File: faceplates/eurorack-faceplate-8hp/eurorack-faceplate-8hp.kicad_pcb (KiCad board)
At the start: 2 copper layers, 40.3 x 133.3 mm, 2 parts

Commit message: Moving mounting holes
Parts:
- added REF**: MountingHole_3.2mm_M3, MountingHole:MountingHole_3.2mm_M3, F.Cu at (35.2, 3.00)
- added REF**: MountingHole_3.2mm_M3, MountingHole:MountingHole_3.2mm_M3, F.Cu at (35.2, 130.3)
- moved REF** 2.42 mm to (5.08, 130.3)
- moved REF** 2.42 mm to (5.08, 3.00)
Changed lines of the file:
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@@
   (net 0 "")
   (footprint "MountingHole:MountingHole_3.2mm_M3" (layer "F.Cu")
-    (at 7.5 130.35)
+    (at 35.22 3)
     (descr "Mounting Hole 3.2mm, no annular, M3")
     (tags "mounting hole 3.2mm no annular m3")
@@
   )
   (footprint "MountingHole:MountingHole_3.2mm_M3" (layer "F.Cu")
-    (at 7.5 3)
+    (at 35.22 130.35)
+    (descr "Mounting Hole 3.2mm, no annular, M3")
+    (tags "mounting hole 3.2mm no annular m3")
+    (attr exclude_from_pos_files exclude_from_bom)
+    (fp_text reference "REF**" (at 0 -4.2) (layer "F.SilkS") hide
+      (effects (font (size 1 1) (thickness 0.15)))
+    )
+    (fp_text value "MountingHole_3.2mm_M3" (at 0 4.2) (layer "F.Fab") hide
+      (effects (font (size 1 1) (thickness 0.15)))
+    )
+    (fp_text user "${REFERENCE}" (at 0.3 0) (layer "F.Fab") hide
+      (effects (font (size 1 1) (thickness 0.15)))
+    )
+    (fp_circle (center 0 0) (end 3.2 0) (layer "Cmts.User") (width 0.15) (fill none))
+    (fp_circle (center 0 0) (end 3.45 0) (layer "F.CrtYd") (width 0.05) (fill none))
+    (pad "" np_thru_hole oval locked (at 0 0) (size 7 3.2) (drill oval 7 3.2) (layers F&B.Cu *.Mask))
+  )
+  (footprint "MountingHole:MountingHole_3.2mm_M3" (layer "F.Cu")
+    (at 5.08 130.35)
+    (descr "Mounting Hole 3.2mm, no annular, M3")
+    (tags "mounting hole 3.2mm no annular m3")
+    (attr exclude_from_pos_files exclude_from_bom)
+    (fp_text reference "REF**" (at 0 -4.2) (layer "F.SilkS") hide
+      (effects (font (size 1 1) (thickness 0.15)))
+    )
+    (fp_text value "MountingHole_3.2mm_M3" (at 0 4.2) (layer "F.Fab") hide
+      (effects (font (size 1 1) (thickness 0.15)))
+    )
+    (fp_text user "${REFERENCE}" (at 0.3 0) (layer "F.Fab") hide
+      (effects (font (size 1 1) (thickness 0.15)))
+    )
+    (fp_circle (center 0 0) (end 3.2 0) (layer "Cmts.User") (width 0.15) (fill none))
+    (fp_circle (center 0 0) (end 3.45 0) (layer "F.CrtYd") (width 0.05) (fill none))
+    (pad "" np_thru_hole oval locked (at 0 0) (size 7 3.2) (drill oval 7 3.2) (layers F&B.Cu *.Mask))
+  )
+  (footprint "MountingHole:MountingHole_3.2mm_M3" (layer "F.Cu")
+    (at 5.08 3)
     (descr "Mounting Hole 3.2mm, no annular, M3")
     (tags "mounting hole 3.2mm no annular m3")
@@
   (gr_line (start 0 0) (end 40.3 0) (layer "Edge.Cuts") (width 0.1))
   (gr_line (start 40.3 133.35) (end 0 133.35) (layer "Edge.Cuts") (width 0.1))
+  (dimension (type aligned) (layer "User.1")
+    (pts (xy 5.08 3) (xy 0 3))
+    (height 7)
+    (gr_text "5.0800 mm" (at 2.54 -5.15) (layer "User.1")
+      (effects (font (size 1 1) (thickness 0.15)))
+    )
+    (format (units 3) (units_format 1) (precision 4))
+    (style (thickness 0.15) (arrow_length 1.27) (text_position_mode 0) (extension_height 0.58642) (extension_offset 0.5) keep_text_aligned)
+  )
 )

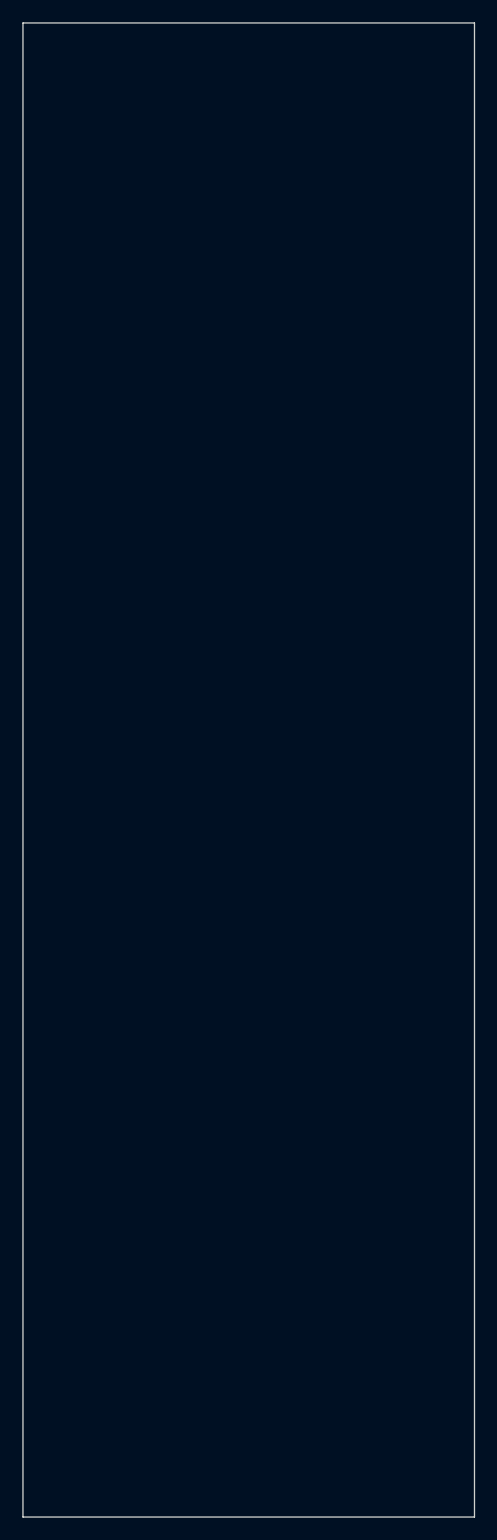
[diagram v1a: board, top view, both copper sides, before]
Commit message: Correcting panel height
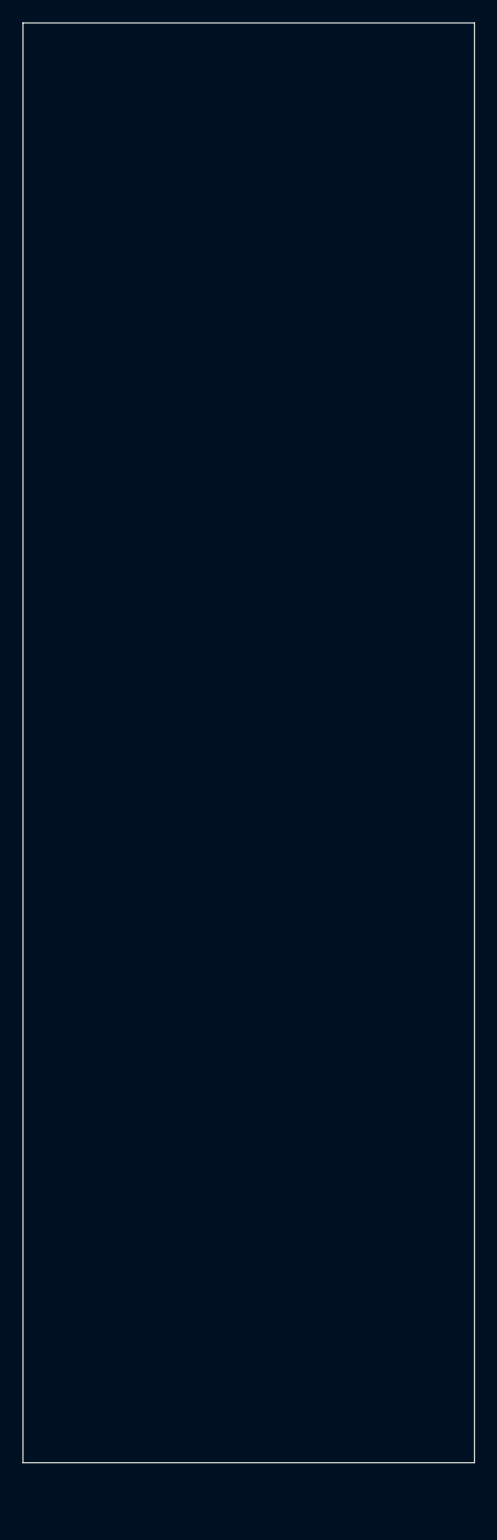
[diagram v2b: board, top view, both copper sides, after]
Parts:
- moved REF** 4.85 mm to (35.2, 125.5)
- moved REF** 4.85 mm to (5.08, 125.5)
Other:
- board size 40.3 x 133.3 mm -> 40.3 x 128.5 mm
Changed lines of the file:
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@@
   )
   (footprint "MountingHole:MountingHole_3.2mm_M3" (layer "F.Cu")
-    (at 35.22 130.35)
+    (at 35.22 125.5)
     (descr "Mounting Hole 3.2mm, no annular, M3")
     (tags "mounting hole 3.2mm no annular m3")
@@
   )
   (footprint "MountingHole:MountingHole_3.2mm_M3" (layer "F.Cu")
-    (at 5.08 130.35)
+    (at 5.08 125.5)
     (descr "Mounting Hole 3.2mm, no annular, M3")
     (tags "mounting hole 3.2mm no annular m3")
@@
     (pad "" np_thru_hole oval locked (at 0 0) (size 7 3.2) (drill oval 7 3.2) (layers F&B.Cu *.Mask))
   )
-  (gr_line (start 40.3 0) (end 40.3 133.35) (layer "Edge.Cuts") (width 0.1))
-  (gr_line (start 0 133.35) (end 0 0) (layer "Edge.Cuts") (width 0.1))
+  (gr_line (start 40.3 0) (end 40.3 128.5) (layer "Edge.Cuts") (width 0.1))
+  (gr_line (start 0 128.5) (end 0 0) (layer "Edge.Cuts") (width 0.1))
   (gr_line (start 0 0) (end 40.3 0) (layer "Edge.Cuts") (width 0.1))
-  (gr_line (start 40.3 133.35) (end 0 133.35) (layer "Edge.Cuts") (width 0.1))
+  (gr_line (start 40.3 128.5) (end 0 128.5) (layer "Edge.Cuts") (width 0.1))
   (dimension (type aligned) (layer "User.1")
     (pts (xy 5.08 3) (xy 0 3))
